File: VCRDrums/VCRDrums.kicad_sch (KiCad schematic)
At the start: 0 parts

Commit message: fixed ugly commit history
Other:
- added sheet Clap (Clap.kicad_sch)
- added sheet HiHats (HiHats.kicad_sch)
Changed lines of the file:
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@@
+		)
+	)
+	(sheet
+		(at 29.972 128.27)
+		(size 43.434 34.29)
+		(fields_autoplaced yes)
+		(stroke
+			(width 0.1524)
+			(type solid)
+		)
+		(fill
+			(color 0 0 0 0.0000)
+		)
+		(property "Sheetname" "Clap"
+			(at 29.972 127.5584 0)
+			(effects
+				(font
+					(size 1.27 1.27)
+				)
+				(justify left bottom)
+			)
+		)
+		(property "Sheetfile" "Clap.kicad_sch"
+			(at 29.972 163.1446 0)
+			(effects
+				(font
+					(size 1.27 1.27)
+				)
+				(justify left top)
+			)
+		)
+		(instances
+			(project "VCRDrums"
+				(path "/35fcb85e-691e-4cf3-b059-6204b1f3c456"
+					(page "7")
+				)
+			)
+		)
+	)
+	(sheet
+		(at 74.93 78.994)
+		(size 48.514 42.164)
+		(fields_autoplaced yes)
+		(stroke
+			(width 0.1524)
+			(type solid)
+		)
+		(fill
+			(color 0 0 0 0.0000)
+		)
+		(property "Sheetname" "HiHats"
+			(at 74.93 78.2824 0)
+			(effects
+				(font
+					(size 1.27 1.27)
+				)
+				(justify left bottom)
+			)
+		)
+		(property "Sheetfile" "HiHats.kicad_sch"
+			(at 74.93 121.7426 0)
+			(effects
+				(font
+					(size 1.27 1.27)
+				)
+				(justify left top)
+			)
+		)
+		(instances
+			(project "VCRDrums"
+				(path "/35fcb85e-691e-4cf3-b059-6204b1f3c456"
+					(page "6")
+				)
+			)
 		)
 	)

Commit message: clave VCA math
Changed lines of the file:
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@@
 	)
 	(sheet
-		(at 29.972 128.27)
+		(at 29.972 125.73)
 		(size 43.434 34.29)
 		(fields_autoplaced yes)
@@
 		)
 		(property "Sheetname" "Clap"
-			(at 29.972 127.5584 0)
+			(at 29.972 125.0184 0)
 			(effects
 				(font
@@
 		)
 		(property "Sheetfile" "Clap.kicad_sch"
-			(at 29.972 163.1446 0)
+			(at 29.972 160.6046 0)
 			(effects
 				(font

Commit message: clave in kicad
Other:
- added sheet Clave (Clave.kicad_sch)
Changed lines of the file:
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@@
+	)
+	(sheet
+		(at 74.93 125.73)
+		(size 48.514 34.29)
+		(fields_autoplaced yes)
+		(stroke
+			(width 0.1524)
+			(type solid)
+		)
+		(fill
+			(color 0 0 0 0.0000)
+		)
+		(property "Sheetname" "Clave"
+			(at 74.93 125.0184 0)
+			(effects
+				(font
+					(size 1.27 1.27)
+				)
+				(justify left bottom)
+			)
+		)
+		(property "Sheetfile" "Clave.kicad_sch"
+			(at 74.93 160.6046 0)
+			(effects
+				(font
+					(size 1.27 1.27)
+				)
+				(justify left top)
+			)
+		)
+		(instances
+			(project "VCRDrums"
+				(path "/35fcb85e-691e-4cf3-b059-6204b1f3c456"
+					(page "8")
+				)
+			)
+		)
 	)
 	(sheet

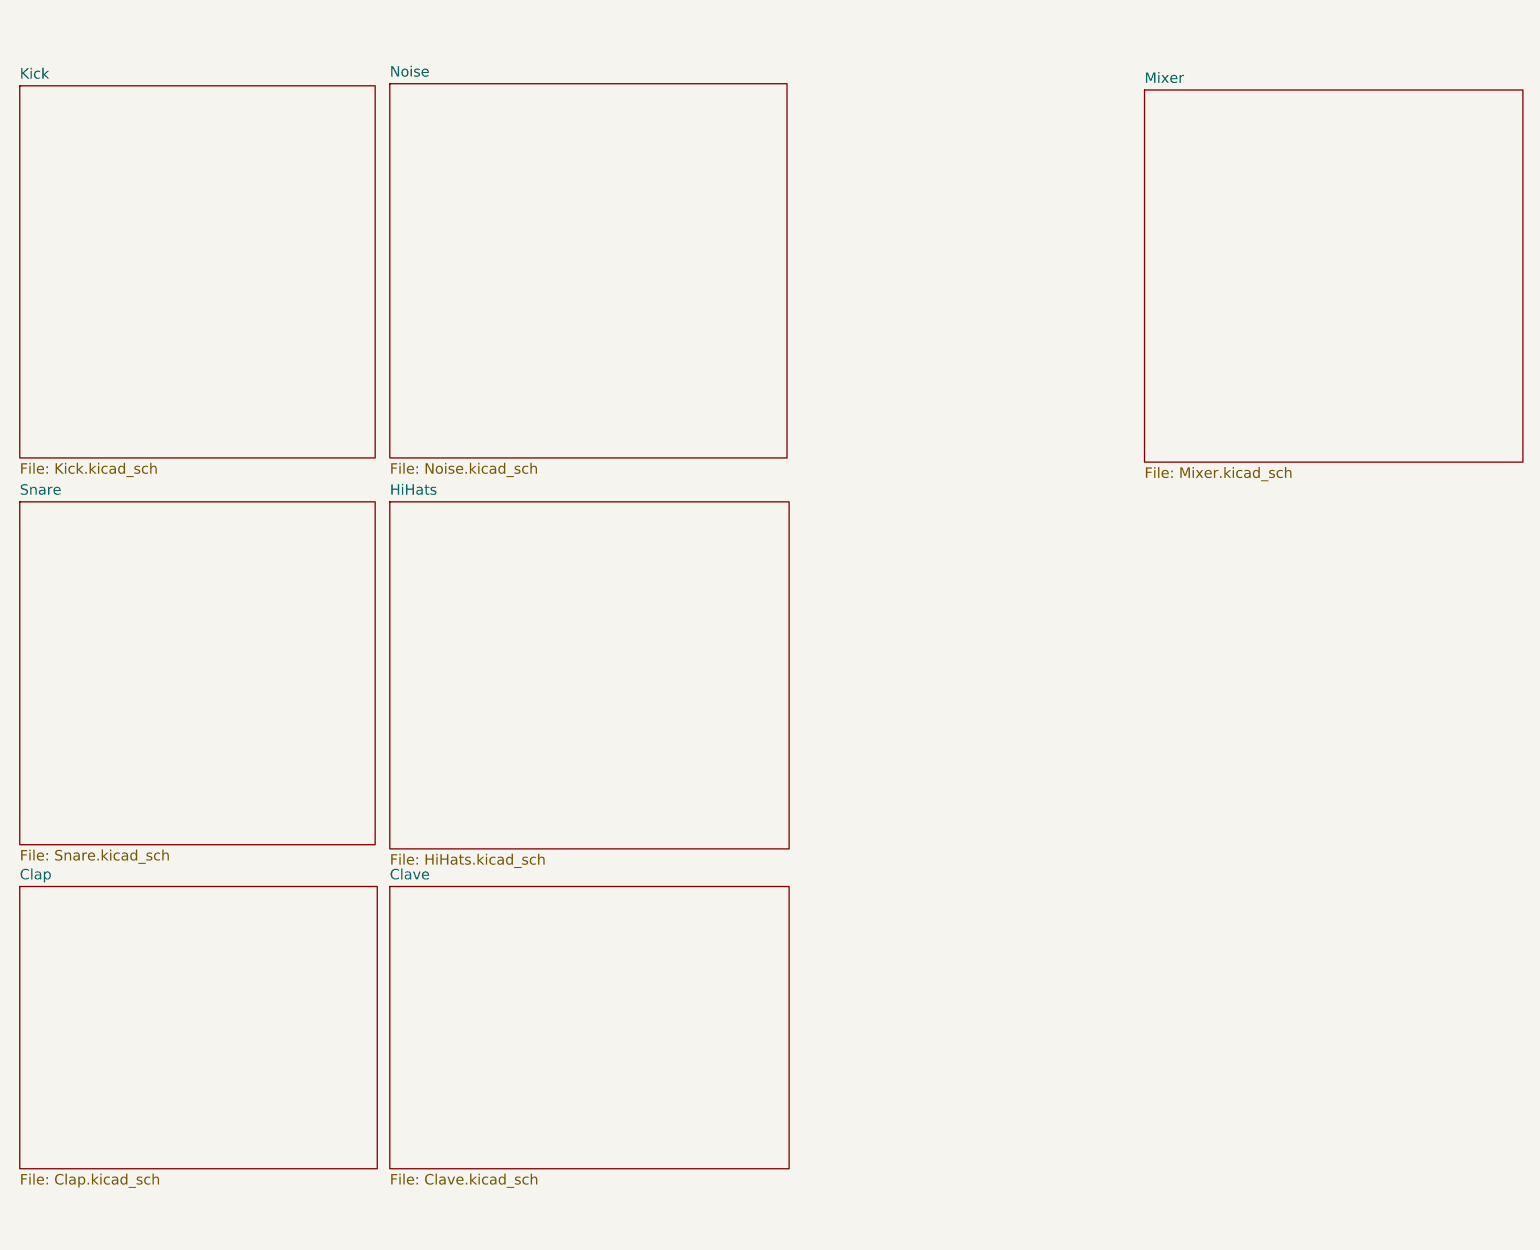
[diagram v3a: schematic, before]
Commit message: mcu skeleton
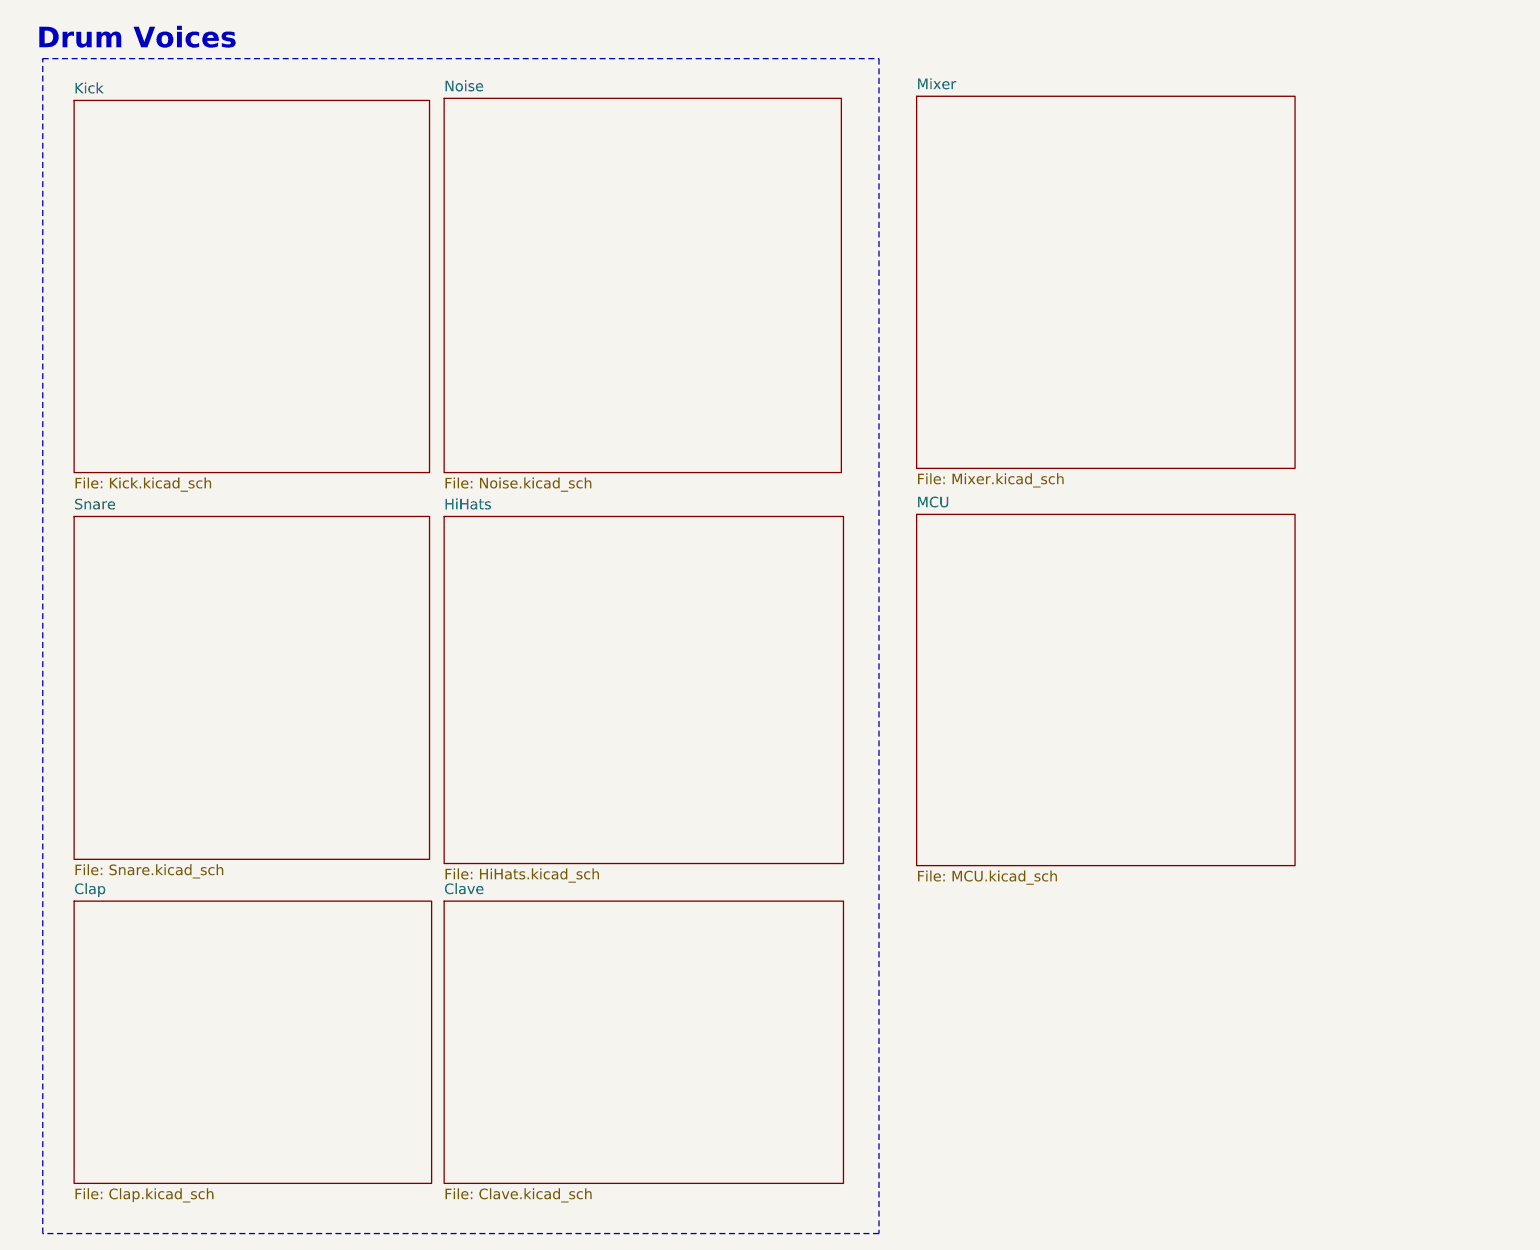
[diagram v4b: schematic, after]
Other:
- added sheet MCU (MCU.kicad_sch)
- note added: "Drum Voices"
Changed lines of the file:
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@@
 	(generator_version "8.0")
 	(paper "A3")
-	(sheet
-		(at 74.93 28.194)
+	(rectangle
+		(start 32.766 25.146)
+		(end 134.366 167.894)
+		(stroke
+			(width 0)
+			(type dash)
+		)
+		(fill
+			(type none)
+		)
+	)
+	(text "Drum Voices"
+		(exclude_from_sim no)
+		(at 44.196 22.86 0)
+		(effects
+			(font
+				(size 2.5 2.5)
+				(thickness 0.5)
+				(bold yes)
+			)
+		)
+	)
+	(sheet
+		(at 138.938 80.518)
+		(size 45.974 42.672)
+		(fields_autoplaced yes)
+		(stroke
+			(width 0.1524)
+			(type solid)
+		)
+		(fill
+			(color 0 0 0 0.0000)
+		)
+		(property "Sheetname" "MCU"
+			(at 138.938 79.8064 0)
+			(effects
+				(font
+					(size 1.27 1.27)
+				)
+				(justify left bottom)
+			)
+		)
+		(property "Sheetfile" "MCU.kicad_sch"
+			(at 138.938 123.7746 0)
+			(effects
+				(font
+					(size 1.27 1.27)
+				)
+				(justify left top)
+			)
+		)
+		(instances
+			(project "VCRDrums"
+				(path "/35fcb85e-691e-4cf3-b059-6204b1f3c456"
+					(page "9")
+				)
+			)
+		)
+	)
+	(sheet
+		(at 81.534 29.972)
 		(size 48.26 45.466)
 		(fields_autoplaced yes)
@@
 		)
 		(property "Sheetname" "Noise"
-			(at 74.93 27.4824 0)
+			(at 81.534 29.2604 0)
 			(effects
 				(font
@@
 		)
 		(property "Sheetfile" "Noise.kicad_sch"
-			(at 74.93 74.2446 0)
+			(at 81.534 76.0226 0)
 			(effects
 				(font
@@
 	)
 	(sheet
-		(at 74.93 125.73)
+		(at 81.534 127.508)
 		(size 48.514 34.29)
 		(fields_autoplaced yes)
@@
 		)
 		(property "Sheetname" "Clave"
-			(at 74.93 125.0184 0)
+			(at 81.534 126.7964 0)
 			(effects
 				(font
@@
 		)
 		(property "Sheetfile" "Clave.kicad_sch"
-			(at 74.93 160.6046 0)
+			(at 81.534 162.3826 0)
 			(effects
 				(font
@@
 	)
 	(sheet
-		(at 29.972 28.448)
+		(at 36.576 30.226)
 		(size 43.18 45.212)
 		(fields_autoplaced yes)
@@
 		)
 		(property "Sheetname" "Kick"
-			(at 29.972 27.7364 0)
+			(at 36.576 29.5144 0)
 			(effects
 				(font
@@
 		)
 		(property "Sheetfile" "Kick.kicad_sch"
-			(at 29.972 74.2446 0)
+			(at 36.576 76.0226 0)
 			(effects
 				(font
@@
 	)
 	(sheet
-		(at 166.624 28.956)
+		(at 138.938 29.718)
 		(size 45.974 45.212)
 		(fields_autoplaced yes)
@@
 		)
 		(property "Sheetname" "Mixer"
-			(at 166.624 28.2444 0)
+			(at 138.938 29.0064 0)
 			(effects
 				(font
@@
 		)
 		(property "Sheetfile" "Mixer.kicad_sch"
-			(at 166.624 74.7526 0)
+			(at 138.938 75.5146 0)
 			(effects
 				(font
@@
 	)
 	(sheet
-		(at 29.972 78.994)
+		(at 36.576 80.772)
 		(size 43.18 41.656)
 		(fields_autoplaced yes)
@@
 		)
 		(property "Sheetname" "Snare"
-			(at 29.972 78.2824 0)
+			(at 36.576 80.0604 0)
 			(effects
 				(font
@@
 		)
 		(property "Sheetfile" "Snare.kicad_sch"
-			(at 29.972 121.2346 0)
+			(at 36.576 123.0126 0)
 			(effects
 				(font
@@
 	)
 	(sheet
-		(at 29.972 125.73)
+		(at 36.576 127.508)
 		(size 43.434 34.29)
 		(fields_autoplaced yes)
@@
 		)
 		(property "Sheetname" "Clap"
-			(at 29.972 125.0184 0)
+			(at 36.576 126.7964 0)
 			(effects
 				(font
@@
 		)
 		(property "Sheetfile" "Clap.kicad_sch"
-			(at 29.972 160.6046 0)
+			(at 36.576 162.3826 0)
 			(effects
 				(font
@@
 	)
 	(sheet
-		(at 74.93 78.994)
+		(at 81.534 80.772)
 		(size 48.514 42.164)
 		(fields_autoplaced yes)
@@
 		)
 		(property "Sheetname" "HiHats"
-			(at 74.93 78.2824 0)
+			(at 81.534 80.0604 0)
 			(effects
 				(font
@@
 		)
 		(property "Sheetfile" "HiHats.kicad_sch"
-			(at 74.93 121.7426 0)
-			(effects
-				(font
+			(at 81.534 123.5206 0)
+			(effects
+				(font

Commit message: compressor schem and schematic
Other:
- added sheet Compressor (Compressor.kicad_sch)
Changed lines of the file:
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@@
+	)
+	(sheet
+		(at 138.938 128.016)
+		(size 46.228 33.782)
+		(fields_autoplaced yes)
+		(stroke
+			(width 0.1524)
+			(type solid)
+		)
+		(fill
+			(color 0 0 0 0.0000)
+		)
+		(property "Sheetname" "Compressor"
+			(at 138.938 127.3044 0)
+			(effects
+				(font
+					(size 1.27 1.27)
+				)
+				(justify left bottom)
+			)
+		)
+		(property "Sheetfile" "Compressor.kicad_sch"
+			(at 138.938 162.3826 0)
+			(effects
+				(font
+					(size 1.27 1.27)
+				)
+				(justify left top)
+			)
+		)
+		(instances
+			(project "VCRDrums"
+				(path "/35fcb85e-691e-4cf3-b059-6204b1f3c456"
+					(page "10")
+				)
+			)
+		)
 	)
 	(sheet
